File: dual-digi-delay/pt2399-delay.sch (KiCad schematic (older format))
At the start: 26 parts, among them Q2 2N3904, U4 PT2399

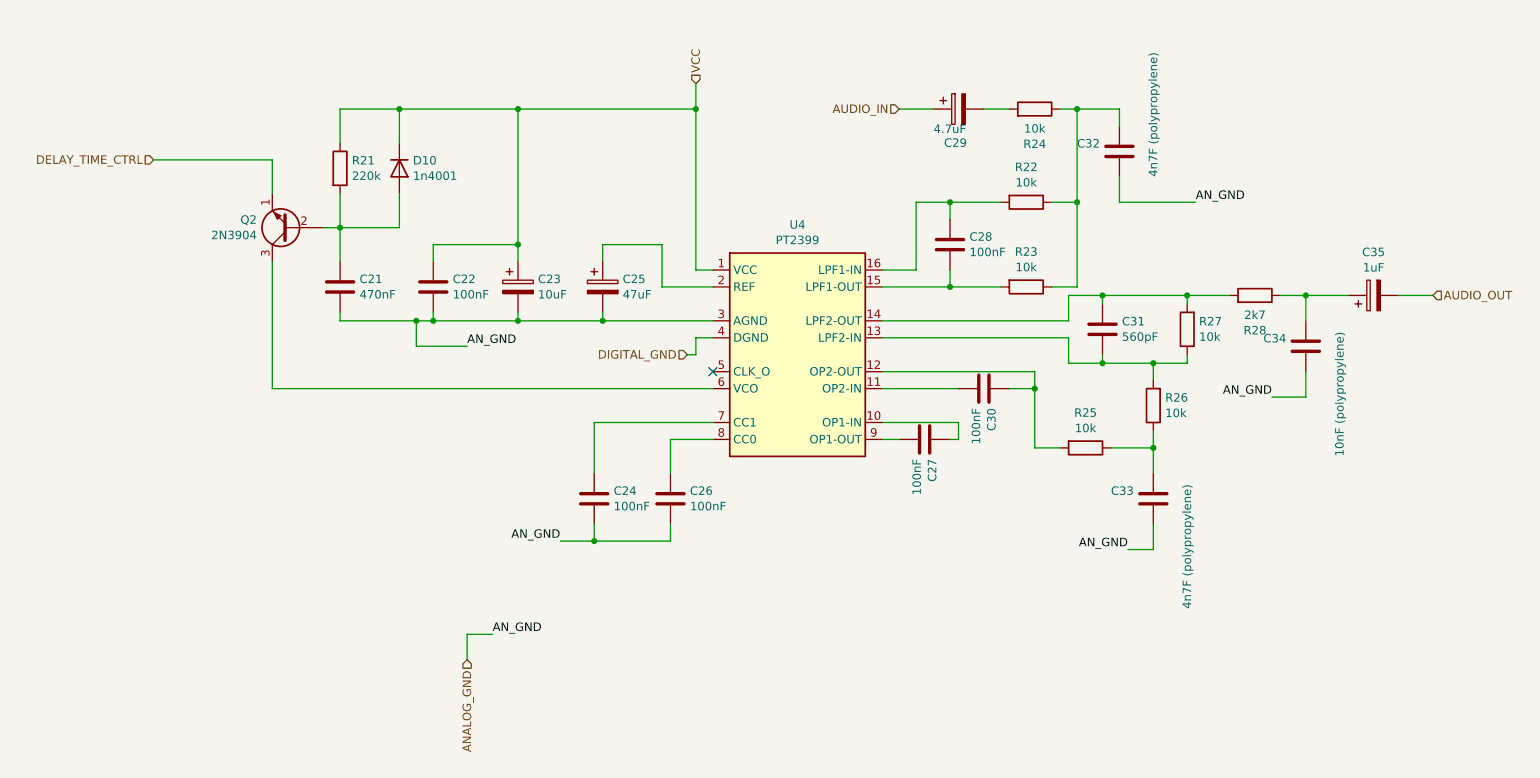
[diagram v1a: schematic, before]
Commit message: Updating digi delay to rev 2
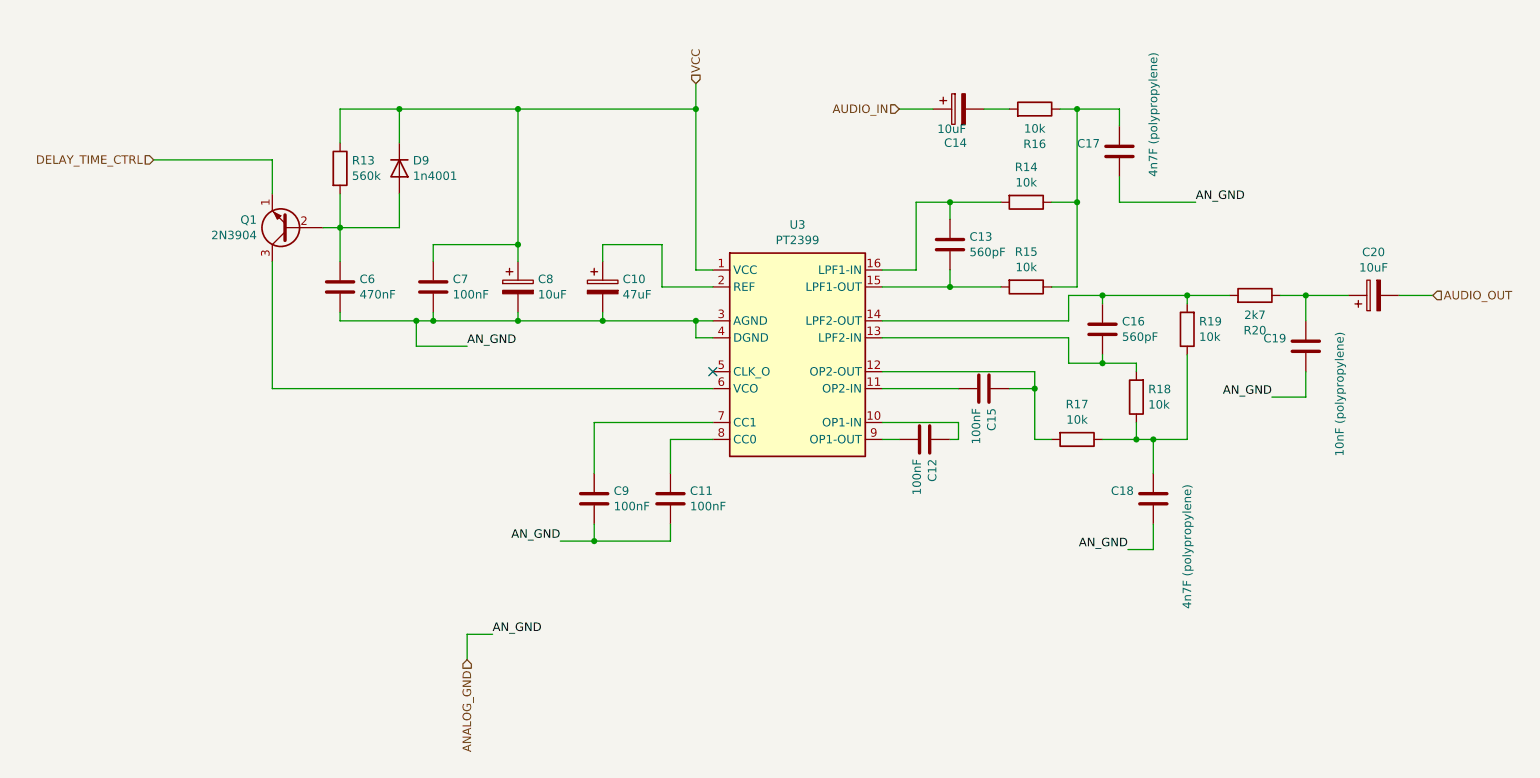
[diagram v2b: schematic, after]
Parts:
- C23: footprint rumblesan-footprints:CP_Radial_D6.3mm_P2.50mm -> rumblesan-footprints:CP_Radial_D5.0mm_P2.50mm
- C28: value 100nF -> 560pF
- C29: value 4.7uF -> 10uF; footprint rumblesan-footprints:CP_Radial_D6.3mm_P2.50mm -> rumblesan-footprints:CP_Radial_D5.0mm_P2.50mm
- C35: value 1uF -> 10uF
- Q2: footprint Package_TO_SOT_THT:TO-92_Inline -> Package_TO_SOT_THT:TO-92_Inline_Wide
- R21: value 220k -> 560k
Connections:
- net DIGITAL_GND is gone; now on net ANALOG_GND: U4.4 (DGND)
- net at C31.2, R26.2, U4.13 (LPF2-IN): no longer R27.1
- net at C33.2, R25.1, R26.1: now also R27.1
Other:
- moved on the sheet: R17, R18
